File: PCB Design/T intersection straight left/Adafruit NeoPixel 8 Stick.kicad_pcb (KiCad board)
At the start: 2 copper layers, 36.6 x 28.6 mm, 8 parts, among them CN1 1X4SMT, CN2 1X4SMT, CN3 1X4SMT

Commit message: t straight fix
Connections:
- CN3 pad 3: Net-(CN3-Pad3) -> GND
- D4 pad 2: Net-(CN3-Pad3) -> unconnected-(D4-Pad2)
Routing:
- net Net-(CN3-Pad3): track 3.24 -> 0.00 mm, vias 1 -> 0
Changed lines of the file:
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@@
   (net 6 "Net-(CN2-Pad3)")
   (net 7 "Net-(D6-Pad2)")
-  (net 8 "Net-(CN3-Pad3)")
+  (net 8 "unconnected-(D4-Pad2)")
   (net 9 "Net-(CN3-Pad4)")
   (net 10 "Net-(D1-Pad2)")
@@
       (net 5 "+5V") (pinfunction "VDD") (pintype "power_in"))
     (pad "2" smd rect (at -2.45 1.6 90) (size 1.5 1) (layers "F.Cu" "F.Paste" "F.Mask")
-      (net 8 "Net-(CN3-Pad3)") (pinfunction "DOUT") (pintype "output"))
+      (net 8 "unconnected-(D4-Pad2)") (pinfunction "DOUT") (pintype "output"))
     (pad "3" smd rect (at 2.45 1.6 90) (size 1.5 1) (layers "F.Cu" "F.Paste" "F.Mask")
       (net 1 "GND") (pinfunction "VSS") (pintype "power_in"))
@@
       (net 3 "Net-(CN1-Pad2)") (pinfunction "2") (pintype "bidirectional") (solder_mask_margin 0.1016))
     (pad "3" smd rect (at -0.92 0 180) (size 1.5 3.8) (layers "B.Cu" "B.Paste" "B.Mask")
-      (net 8 "Net-(CN3-Pad3)") (pinfunction "3") (pintype "bidirectional") (solder_mask_margin 0.1016))
+      (net 1 "GND") (pinfunction "3") (pintype "bidirectional") (solder_mask_margin 0.1016))
     (pad "4" smd rect (at 2.08 0 180) (size 1.5 3.8) (layers "B.Cu" "B.Paste" "B.Mask")
       (net 9 "Net-(CN3-Pad4)") (pinfunction "4") (pintype "bidirectional") (solder_mask_margin 0.1016))
@@
   (segment (start 149.421782 103.217041) (end 149.421782 106.481782) (width 0.25) (layer "F.Cu") (net 7))
   (segment (start 149.421782 106.481782) (end 151.982 109.042) (width 0.25) (layer "F.Cu") (net 7))
-  (segment (start 142.316 97.446) (end 142.316 94.31) (width 0.25) (layer "F.Cu") (net 8))
-  (segment (start 142.316 94.31) (end 142.24 94.234) (width 0.25) (layer "F.Cu") (net 8))
-  (via (at 142.24 94.234) (size 0.8) (drill 0.4) (layers "F.Cu" "B.Cu") (net 8))
   (via (at 139.192 92.71) (size 0.8) (drill 0.4) (layers "F.Cu" "B.Cu") (net 9))
   (segment (start 129.704 105.842) (end 134.164741 105.842) (width 0.25) (layer "F.Cu") (net 10))

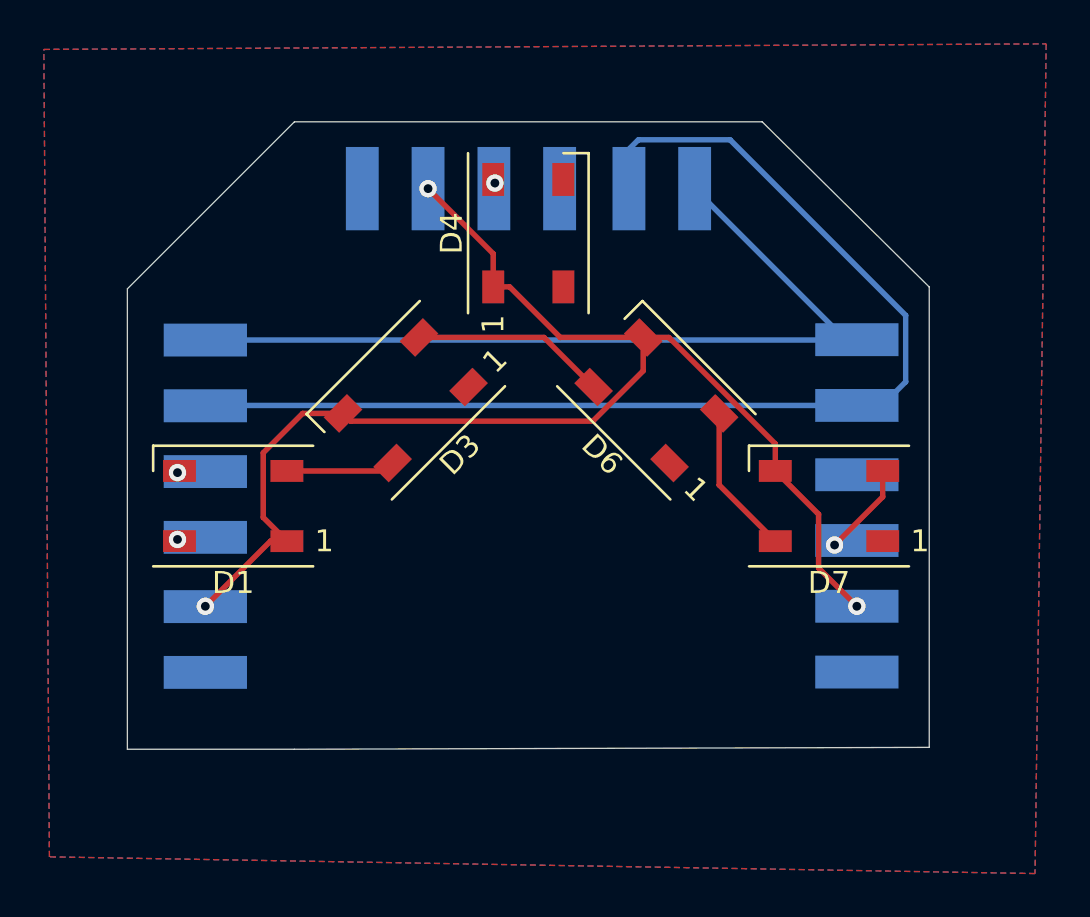
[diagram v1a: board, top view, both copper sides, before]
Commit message: move vias off pads
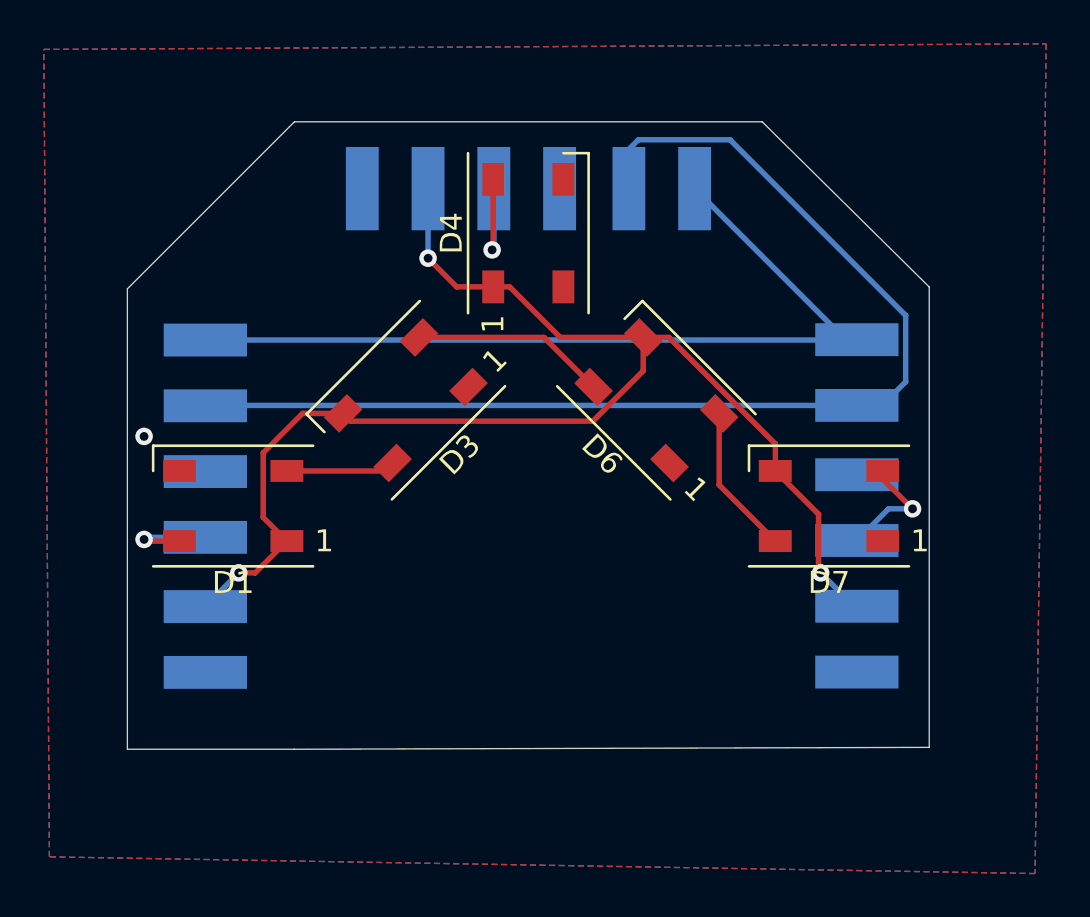
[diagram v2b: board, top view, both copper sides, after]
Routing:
- net Net-(CN3-Pad4): track 0.00 -> 6.06 mm
- net Net-(CN2-Pad3): track 0.00 -> 4.48 mm
- net Net-(CN1-Pad4): track 4.29 -> 5.43 mm
- net +5V: track 60.6 -> 61.4 mm
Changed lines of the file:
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@@
   (gr_line locked (start 122.428 118.536) (end 130.048 118.536) (layer "Edge.Cuts") (width 0.05))
   (gr_line (start 122.428 97.536) (end 130.048 89.915998) (layer "Edge.Cuts") (width 0.05))
-  (via (at 124.714 105.918) (size 0.8) (drill 0.4) (layers "F.Cu" "B.Cu") (net 1))
+  (via (at 123.19 104.267) (size 0.8) (drill 0.4) (layers "F.Cu" "B.Cu") (free) (net 1))
   (segment (start 125.984 99.87) (end 155.686 99.87) (width 0.25) (layer "B.Cu") (net 2))
   (segment (start 155.686 99.87) (end 155.702 99.854) (width 0.25) (layer "B.Cu") (net 2))
@@
   (segment (start 157.9302 101.7758) (end 157.9302 98.7482) (width 0.25) (layer "B.Cu") (net 3))
   (segment (start 149.9178 90.7358) (end 145.7382 90.7358) (width 0.25) (layer "B.Cu") (net 3))
-  (segment (start 156.882 107.024) (end 154.686 109.22) (width 0.25) (layer "F.Cu") (net 4))
-  (segment (start 156.882 105.842) (end 156.882 107.024) (width 0.25) (layer "F.Cu") (net 4))
-  (via (at 154.686 109.22) (size 0.8) (drill 0.4) (layers "F.Cu" "B.Cu") (net 4))
-  (segment (start 139.116 97.446) (end 139.116 95.936) (width 0.25) (layer "F.Cu") (net 5))
+  (segment (start 156.882 106.209) (end 158.242 107.569) (width 0.25) (layer "F.Cu") (net 4))
+  (segment (start 156.882 105.842) (end 156.882 106.209) (width 0.25) (layer "F.Cu") (net 4))
+  (via (at 158.242 107.569) (size 0.8) (drill 0.4) (layers "F.Cu" "B.Cu") (net 4))
+  (segment (start 155.702 109.014) (end 157.147 107.569) (width 0.25) (layer "B.Cu") (net 4))
+  (segment (start 157.147 107.569) (end 158.242 107.569) (width 0.25) (layer "B.Cu") (net 4))
   (segment (start 128.6258 107.9638) (end 129.704 109.042) (width 0.25) (layer "F.Cu") (net 5))
   (segment (start 151.982 105.842) (end 153.9578 107.8178) (width 0.25) (layer "F.Cu") (net 5))
+  (segment (start 127.508 110.49) (end 128.256 110.49) (width 0.25) (layer "F.Cu") (net 5))
   (segment (start 145.956959 99.752218) (end 147.128211 99.752218) (width 0.25) (layer "F.Cu") (net 5))
   (segment (start 139.866 97.446) (end 142.172218 99.752218) (width 0.25) (layer "F.Cu") (net 5))
+  (segment (start 128.256 110.49) (end 129.704 109.042) (width 0.25) (layer "F.Cu") (net 5))
   (segment (start 132.617771 103.570594) (end 132.264218 103.217041) (width 0.25) (layer "F.Cu") (net 5))
   (segment (start 145.956959 101.277024) (end 143.663389 103.570594) (width 0.25) (layer "F.Cu") (net 5))
-  (segment (start 129.704 109.042) (end 128.956 109.042) (width 0.25) (layer "F.Cu") (net 5))
-  (segment (start 153.9578 110.2698) (end 155.702 112.014) (width 0.25) (layer "F.Cu") (net 5))
+  (segment (start 139.116 97.446) (end 137.451 97.446) (width 0.25) (layer "F.Cu") (net 5))
   (segment (start 147.128211 99.752218) (end 151.982 104.606007) (width 0.25) (layer "F.Cu") (net 5))
   (segment (start 142.172218 99.752218) (end 145.956959 99.752218) (width 0.25) (layer "F.Cu") (net 5))
   (segment (start 132.264218 103.217041) (end 130.422559 103.217041) (width 0.25) (layer "F.Cu") (net 5))
-  (segment (start 139.116 95.936) (end 136.144 92.964) (width 0.25) (layer "F.Cu") (net 5))
   (segment (start 143.663389 103.570594) (end 132.617771 103.570594) (width 0.25) (layer "F.Cu") (net 5))
   (segment (start 151.982 104.606007) (end 151.982 105.842) (width 0.25) (layer "F.Cu") (net 5))
   (segment (start 128.6258 105.0138) (end 128.6258 107.9638) (width 0.25) (layer "F.Cu") (net 5))
   (segment (start 130.422559 103.217041) (end 128.6258 105.0138) (width 0.25) (layer "F.Cu") (net 5))
+  (segment (start 137.451 97.446) (end 136.144 96.139) (width 0.25) (layer "F.Cu") (net 5))
   (segment (start 153.9578 107.8178) (end 153.9578 110.2698) (width 0.25) (layer "F.Cu") (net 5))
-  (segment (start 128.956 109.042) (end 125.984 112.014) (width 0.25) (layer "F.Cu") (net 5))
   (segment (start 145.956959 99.752218) (end 145.956959 101.277024) (width 0.25) (layer "F.Cu") (net 5))
   (segment (start 139.116 97.446) (end 139.866 97.446) (width 0.25) (layer "F.Cu") (net 5))
-  (via (at 155.702 112.014) (size 0.8) (drill 0.4) (layers "F.Cu" "B.Cu") (net 5))
-  (via (at 136.144 92.964) (size 0.8) (drill 0.4) (layers "F.Cu" "B.Cu") (net 5))
-  (via (at 125.984 112.014) (size 0.8) (drill 0.4) (layers "F.Cu" "B.Cu") (net 5))
-  (via (at 124.714 108.966) (size 0.8) (drill 0.4) (layers "F.Cu" "B.Cu") (net 6))
+  (via (at 154.051 110.49) (size 0.8) (drill 0.4) (layers "F.Cu" "B.Cu") (net 5))
+  (via (at 136.144 96.139) (size 0.8) (drill 0.4) (layers "F.Cu" "B.Cu") (net 5))
+  (via (at 127.508 110.49) (size 0.8) (drill 0.4) (layers "F.Cu" "B.Cu") (net 5))
+  (segment (start 155.575 112.014) (end 154.051 110.49) (width 0.25) (layer "B.Cu") (net 5))
+  (segment (start 155.702 112.014) (end 155.575 112.014) (width 0.25) (layer "B.Cu") (net 5))
+  (segment (start 136.144 92.964) (end 136.144 96.139) (width 0.25) (layer "B.Cu") (net 5))
+  (segment (start 125.984 112.014) (end 127.508 110.49) (width 0.25) (layer "B.Cu") (net 5))
+  (segment (start 125.984 112.03) (end 125.984 112.014) (width 0.25) (layer "B.Cu") (net 5))
+  (segment (start 124.804 109.042) (end 123.266 109.042) (width 0.25) (layer "F.Cu") (net 6))
+  (segment (start 123.266 109.042) (end 123.19 108.966) (width 0.25) (layer "F.Cu") (net 6))
+  (via (at 123.19 108.966) (size 0.8) (drill 0.4) (layers "F.Cu" "B.Cu") (net 6))
+  (segment (start 123.286 108.87) (end 123.19 108.966) (width 0.25) (layer "B.Cu") (net 6))
+  (segment (start 125.984 108.87) (end 123.286 108.87) (width 0.25) (layer "B.Cu") (net 6))
   (segment (start 149.421782 103.217041) (end 149.421782 106.481782) (width 0.25) (layer "F.Cu") (net 7))
   (segment (start 149.421782 106.481782) (end 151.982 109.042) (width 0.25) (layer "F.Cu") (net 7))
-  (via (at 139.192 92.71) (size 0.8) (drill 0.4) (layers "F.Cu" "B.Cu") (net 9))
+  (segment (start 139.116 95.707) (end 139.065 95.758) (width 0.25) (layer "F.Cu") (net 9))
+  (segment (start 139.116 92.546) (end 139.116 95.707) (width 0.25) (layer "F.Cu") (net 9))
+  (via (at 139.065 95.758) (size 0.8) (drill 0.4) (layers "F.Cu" "B.Cu") (net 9))
+  (segment (start 139.144 92.964) (end 139.144 95.679) (width 0.25) (layer "B.Cu") (net 9))
+  (segment (start 139.144 95.679) (end 139.065 95.758) (width 0.25) (layer "B.Cu") (net 9))
   (segment (start 129.704 105.842) (end 134.164741 105.842) (width 0.25) (layer "F.Cu") (net 10))
   (segment (start 141.431477 99.752218) (end 143.694218 102.014959) (width 0.25) (layer "F.Cu") (net 11))
